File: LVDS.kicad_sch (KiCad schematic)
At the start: 3 parts, among them U6 USBLC6-2SC6

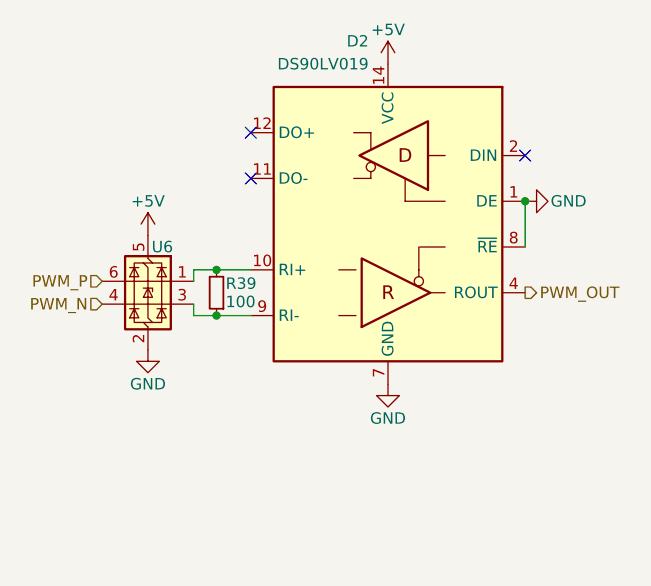
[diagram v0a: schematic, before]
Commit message: VER1.0: добавил разъем под FFC
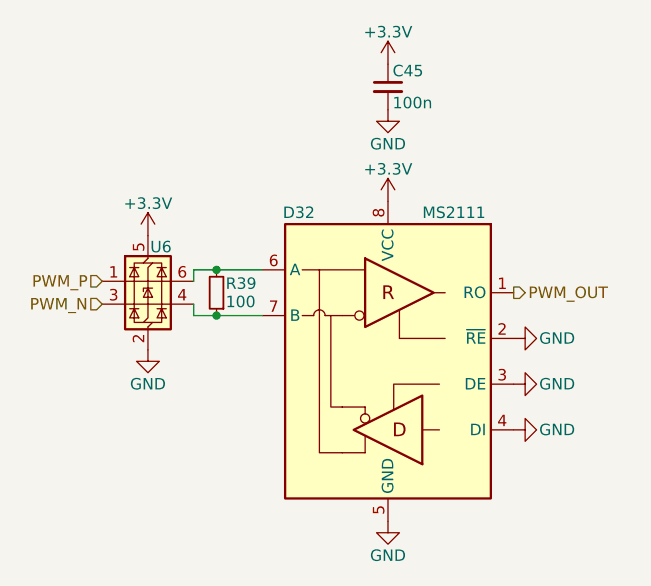
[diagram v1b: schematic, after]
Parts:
- removed D2: DS90LV019, Package_SO:SO-14_3.9x8.65mm_P1.27mm, symbol Interface_my:DS90L019TMx
- added C45: 100n, Capacitor_SMD:C_0805_2012Metric_Pad1.18x1.45mm_HandSolder, symbol Device:C_Small
- added D32: MS2111, Package_SO:SO-8_3.9x4.9mm_P1.27mm, symbol Interface_my:MS2111
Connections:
- net GND: now also C45.2, D32.2 (~{RE}), D32.3 (DE), D32.4 (DI), D32.5 (GND)
- net PWM_N: now also U6.3 (I/O2); no longer U6.4 (I/O2)
- net PWM_OUT: now also D32.1 (RO)
- net PWM_P: now also U6.1 (I/O1); no longer U6.6 (I/O1)
- net at R39.1: now also U6.4 (I/O2), D32.7 (B); no longer U6.3 (I/O2)
- net at R39.2: now also U6.6 (I/O1), D32.6 (NC); no longer U6.1 (I/O1)
- net +5V renamed +3.3V
- net +3.3V: now also C45.1, D32.8 (VCC)
- no-connect marks 3 -> 0

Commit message: VER1.0: сделал файлы для производства
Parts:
- C45: Description P/N Capacitor SMD 25+V -> Capacitor SMD 50V
- D32: value MS2111 -> (none); Description P/N (none) -> LVDS; Product Name (none) -> MS2111
- U6: value USBLC6-2SC6 -> (none); Description P/N (none) -> ESD protection; Product Name (none) -> USBLC6-2SC6
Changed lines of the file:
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@@
 			)
 		)
-		(property "Description P/N" "Capacitor SMD 25+V"
+		(property "Description P/N" "Capacitor SMD 50V"
 			(at 149.86 81.28 0)
 			(hide yes)
@@
 			)
 		)
-		(property "Value" "MS2111"
+		(property "Value" ""
 			(at 153.67 95.25 0)
 			(show_name no)
@@
 		)
 		(property "Description" ""
+			(at 149.86 96.52 0)
+			(hide yes)
+			(show_name no)
+			(do_not_autoplace no)
+			(effects
+				(font
+					(size 1.27 1.27)
+				)
+			)
+		)
+		(property "Product Name" "MS2111"
+			(at 149.86 96.52 0)
+			(hide yes)
+			(show_name no)
+			(do_not_autoplace no)
+			(effects
+				(font
+					(size 1.27 1.27)
+				)
+			)
+		)
+		(property "Description P/N" "LVDS"
+			(at 149.86 96.52 0)
+			(hide yes)
+			(show_name no)
+			(do_not_autoplace no)
+			(effects
+				(font
+					(size 1.27 1.27)
+				)
+			)
+		)
+		(property "Replacement" ""
+			(at 149.86 96.52 0)
+			(hide yes)
+			(show_name no)
+			(do_not_autoplace no)
+			(effects
+				(font
+					(size 1.27 1.27)
+				)
+			)
+		)
+		(property "Function" ""
 			(at 149.86 96.52 0)
 			(hide yes)
@@
 			)
 		)
-		(property "Value" "USBLC6-2SC6"
+		(property "Value" ""
 			(at 124.8411 97.79 0)
 			(hide yes)
@@
 			(at 123.19 102.87 0)
 			(hide yes)
+			(show_name no)
+			(do_not_autoplace no)
+			(effects
+				(font
+					(size 1.27 1.27)
+				)
+			)
+		)
+		(property "Product Name" "USBLC6-2SC6"
+			(at 123.19 102.87 0)
+			(hide yes)
+			(show_name no)
+			(do_not_autoplace no)
+			(effects
+				(font
+					(size 1.27 1.27)
+				)
+			)
+		)
+		(property "Description P/N" "ESD protection"
+			(at 123.19 102.87 0)
+			(hide yes)
+			(show_name no)
+			(do_not_autoplace no)
+			(effects
+				(font
+					(size 1.27 1.27)
+				)
+			)
+		)
+		(property "Replacement" ""
+			(at 123.19 102.87 0)
+			(hide yes)
+			(show_name no)
+			(do_not_autoplace no)
+			(effects
+				(font
+					(size 1.27 1.27)
+				)
+			)
+		)
+		(property "Function" ""
+			(at 123.19 102.87 0)
+			(hide yes)
